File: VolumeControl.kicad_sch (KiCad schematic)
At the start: 15 parts

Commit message: some corrections
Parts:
- added C? (x2): C_Polarized 10µF 50V, symbol Device:C_Polarized
- J?: value I2C -> SPI; symbol Connector_Generic:Conn_01x02 -> Connector_Generic:Conn_01x04
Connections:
- net CLK: now also J?.1 (Pin_1), U?.5 (CLK), U?.5 (CLK)
- net GND: now also R?.1, U?.1 (B1), U?.1 (B1), U?.2 (-), U?.2 (GND), U?.2 (GND), U?.6 (-); no longer U?.3 (+)
- net SDA: now also J?.2 (Pin_2)
- net at R?.1, R?.2: now also C?.1; no longer J?.1 (Pin_1) (x2)
- net at J?.1 (Pin_1): now also C?.1; no longer U?.8 (A1)
- net at J?.3 (Pin_3): now also C?.1; no longer U?.8 (A1)
- net at C?.2: now also J?.1 (Pin_1); no longer R?.2 (x2)
- net at U?.7 (W1): now also U?.3 (+); no longer U?.2 (-)
- net SDI: now reaches U?.4 (SDI)
- net SDI: now also U?.4 (SDI)
- net at U?.7 (W1): now also U?.5 (+); no longer U?.6 (-)
- net at U?.7: now also R?.2; no longer C?.1
- new net: C?.2, U?.8 (A1) (x2)
- new net: R?.2, U?.1
- new net CS1: J?.3 (Pin_3), U?.3 (CS*)
- new net CS2: J?.4 (Pin_4), U?.3 (CS*)
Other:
- moved on the sheet: C?, R?

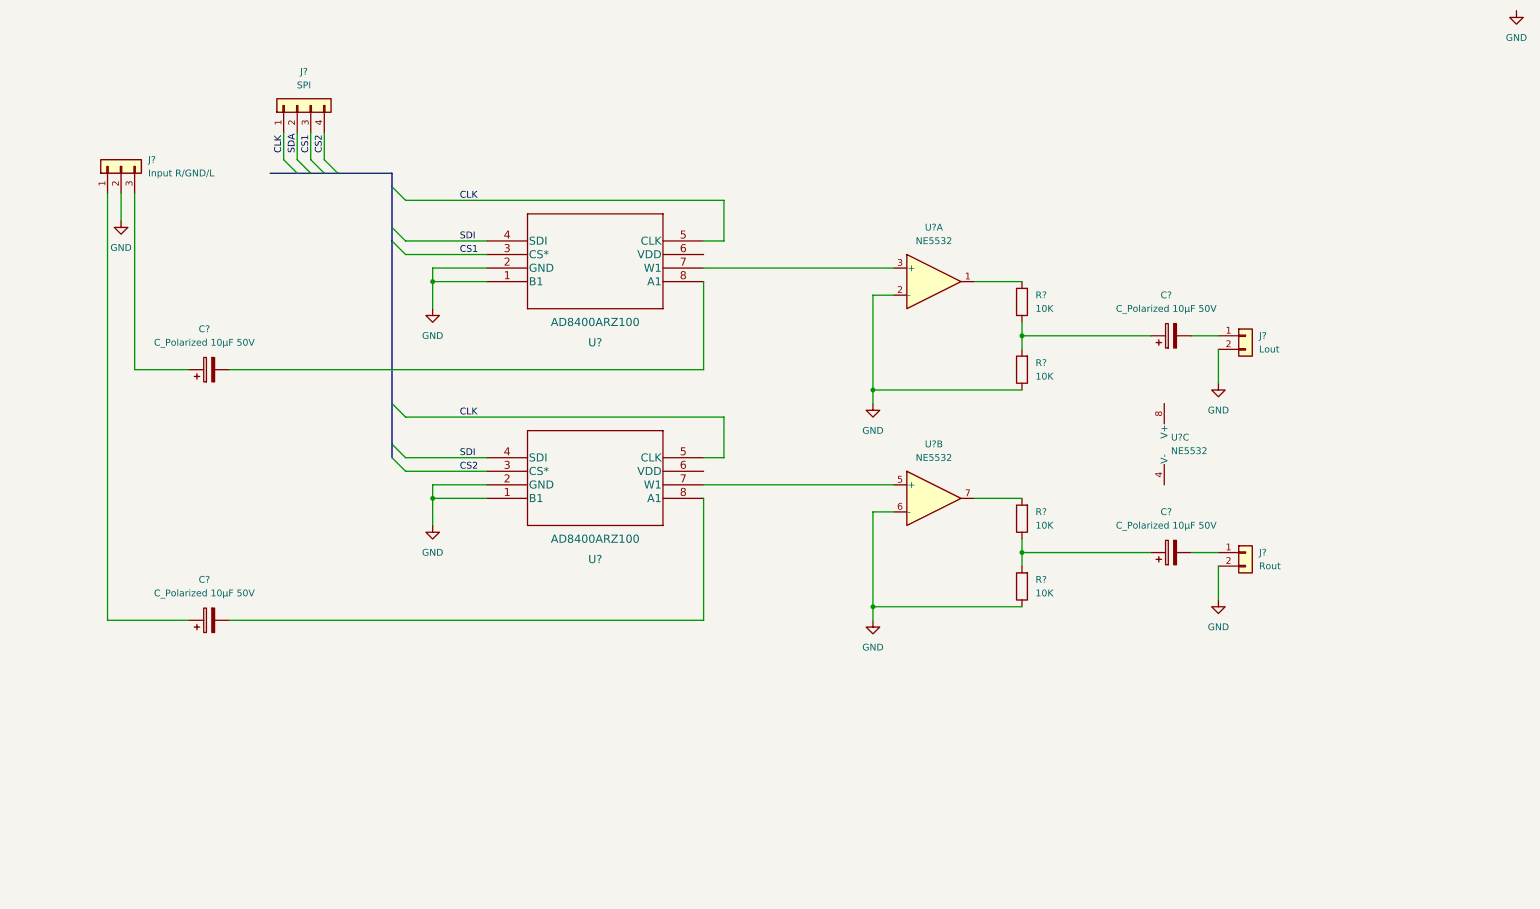
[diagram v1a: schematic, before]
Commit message: Added Sub Out
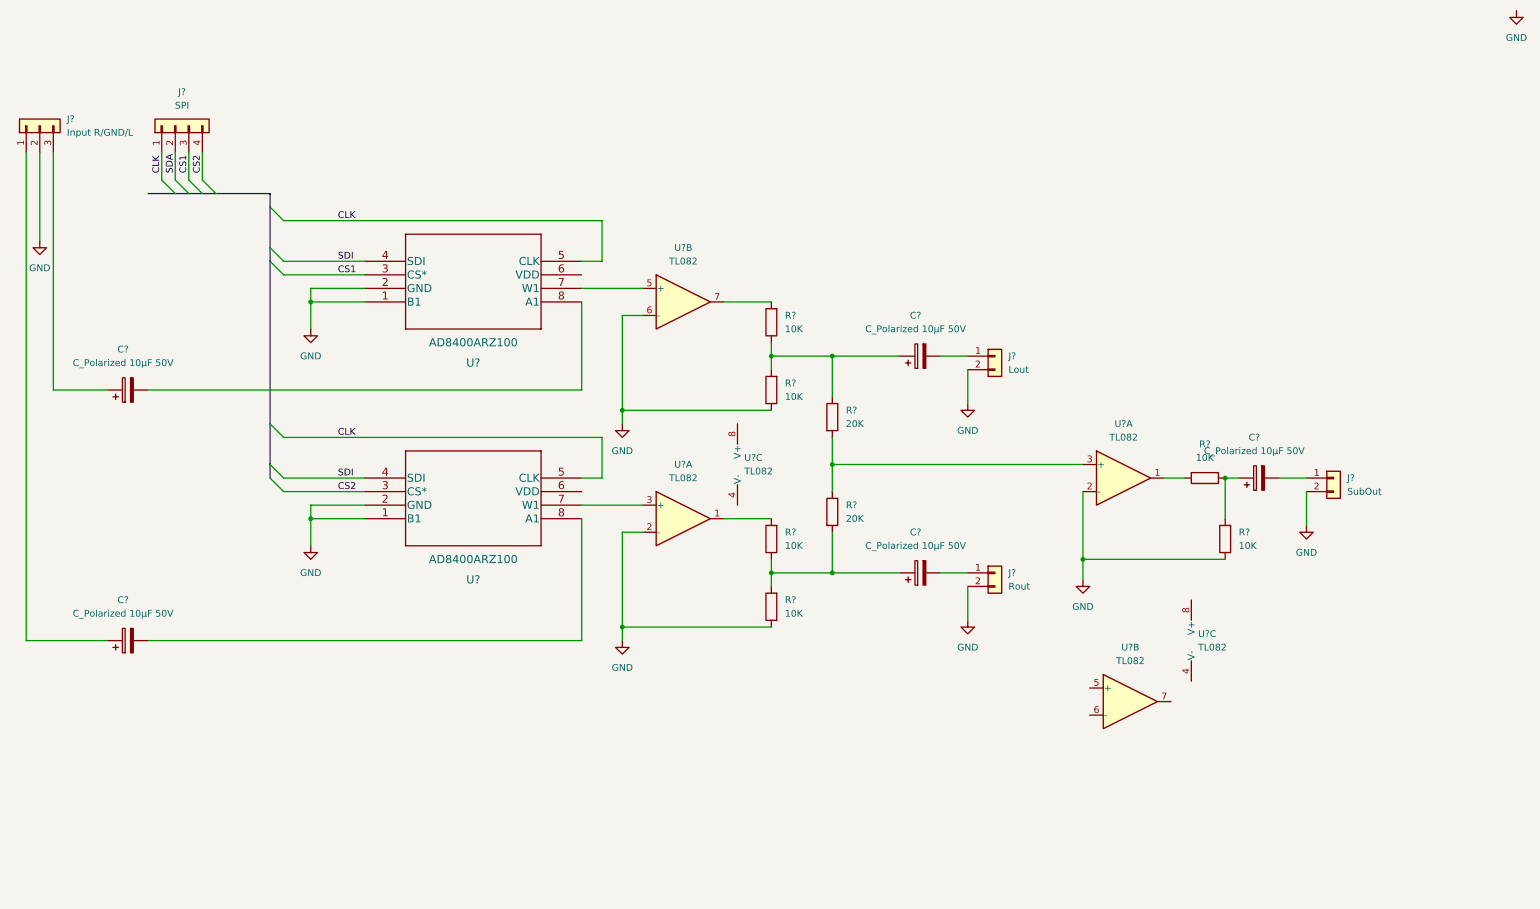
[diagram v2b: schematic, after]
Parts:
- removed U? (x3): NE5532, symbol Amplifier_Operational:NE5532
- added C?: C_Polarized 10µF 50V, symbol Device:C_Polarized
- added J?: SubOut, symbol Connector_Generic:Conn_01x02
- added R? (x2): 20K, symbol Device:R
- added R? (x2): 10K, symbol Device:R
- added U? (x6): TL082, symbol Amplifier_Operational:TL082
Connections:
- net GND: now also J?.2 (Pin_2), R?.1, U?.2 (-), U?.2 (-), U?.6 (-)
- net at C?.1, R?.1, R?.2: now also R?.1
- net at R?.2: now also U?.7
- net at U?.7 (W1): now also U?.5 (+)
- net at U?.7 (W1): now also U?.3 (+)
- net at R?.2: now also U?.1
- net at C?.1, R?.1, R?.2: now also R?.2
- new net: R?.1, R?.2, U?.3 (+)
- new net: C?.2, J?.1 (Pin_1)
- new net: C?.1, R?.1, R?.2
- new net: R?.2, U?.1
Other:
- moved on the sheet: C?, J?, R?, U?

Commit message: Added Power
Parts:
- added J?: Input R/GND/L, symbol Connector_Generic:Conn_01x03
- added J?: DP1 2.7V - 5.5V, symbol Connector_Generic:Conn_01x02
- added J?: DP2 2.7V - 5.5V, symbol Connector_Generic:Conn_01x02
- added JP?: Double or Single PSU, symbol Jumper:Jumper_3_Bridged12
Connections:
- net GND: now also J?.1 (Pin_1), J?.1 (Pin_1), J?.2 (Pin_2)
- net -2.25-40: now reaches U?.4 (V-)
- net -2.25-40: now also U?.4 (V-), J?.1 (Pin_1)
- net +2.25-40: now reaches U?.8 (V+)
- net +2.25-40: now also U?.8 (V+), J?.3 (Pin_3)
- net DP2VDD: now reaches U?.6 (VDD)
- net DP2VDD: now also JP?.2 (C)
- net DP1VDD: now reaches U?.6 (VDD)
- net DP1VDD: now also J?.2 (Pin_2), JP?.1 (A)
- new net: J?.2 (Pin_2), JP?.3 (B)

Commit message: corrected schematic, selected footprints, created pcb file
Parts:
- removed J?: Input R/GND/L, symbol Connector_Generic:Conn_01x03
- removed J?: DP2 2.7V - 5.5V, symbol Connector_Generic:Conn_01x02
- removed JP?: Double or Single PSU, symbol Jumper:Jumper_3_Bridged12
- removed R?: 10K, symbol Device:R
- added C11, C3, C9: 100n, Capacitor_THT:C_Rect_L4.6mm_W2.0mm_P2.50mm_MKS02_FKP02, symbol Device:C
- added C4, C7, C8: 1u, Capacitor_THT:C_Rect_L7.0mm_W2.5mm_P5.00mm, symbol Device:C
- added PS1: IH0512S, Converter_DCDC:Converter_DCDC_XP_POWER-IHxxxxS_THT, symbol Converter_DCDC:IH0512S
- added R1, R2, R3, R4: 100k, Resistor_THT:R_Axial_DIN0207_L6.3mm_D2.5mm_P10.16mm_Horizontal, symbol Device:R
- added R12, R13, R7: 100, Resistor_THT:R_Axial_DIN0207_L6.3mm_D2.5mm_P10.16mm_Horizontal, symbol Device:R
- C1, C10, C2, C5, C6: renamed from C?; footprint (none) -> Capacitor_THT:CP_Radial_D5.0mm_P2.00mm
- J1: renamed from J?; footprint (none) -> Connector_JST:JST_XH_B3B-XH-A_1x03_P2.50mm_Vertical
- J2: renamed from J?; footprint (none) -> Connector_PinHeader_2.54mm:PinHeader_1x04_P2.54mm_Vertical
- J4: renamed from J?; value DP1 2.7V - 5.5V -> 5V Supply; footprint (none) -> Connector_PinHeader_2.54mm:PinHeader_1x02_P2.54mm_Vertical
- J5, J6, J7: renamed from J?; footprint (none) -> Connector_Molex:Molex_KK-254_AE-6410-02A_1x02_P2.54mm_Vertical
- R10, R11, R14: renamed from R?; footprint (none) -> Resistor_THT:R_Axial_DIN0207_L6.3mm_D2.5mm_P10.16mm_Horizontal
- R5, R6: renamed from R?; value 10K -> 12k; footprint (none) -> Resistor_THT:R_Axial_DIN0207_L6.3mm_D2.5mm_P10.16mm_Horizontal
- R8, R9: renamed from R?; value 10K -> 47k; footprint (none) -> Resistor_THT:R_Axial_DIN0207_L6.3mm_D2.5mm_P10.16mm_Horizontal
- U1, U2: renamed from U?; footprint R_8_ADI -> Package_SO:SO-8_3.9x4.9mm_P1.27mm
- U3, U4: renamed from U?; footprint (none) -> Package_DIP:DIP-8_W7.62mm_Socket
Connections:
- net DP2VDD is gone; now on net +5V: U2.6 (VDD)
- net GND: now also C3.2, C4.2, C7.2, C8.1, PS1.2 (-Vin), PS1.5 (0V), R2.1; no longer U3.2 (-), U3.6 (-)
- net at C5.1, R10.1: now also R8.2, U3.7; no longer R5.2, R8.1
- net at C2.2, U2.8 (A1): now also R4.2
- net at R9.2, U3.1: now also C6.1, R11.2
- net at C10.1, R14.2: now also U4.1
- net at C1.2, U1.8 (A1): now also R3.1
- net at R6.2, R9.1: now also U3.2 (-); no longer C6.1, R11.2
- net -12VA: now reaches U4.5 (+)
- net -12VA: now also C8.2, R13.2
- net +12VA: now reaches U4.6 (-)
- net +12VA: now also C7.1, R12.1
- net +2.25-40: no longer names the net of U3.8 (V+), U4.8 (V+)
- net +2.25-40: now also C11.1, C9.1
- net -2.25-40: no longer names the net of U3.4 (V-), U4.4 (V-)
- net -2.25-40: now also C11.2, C9.2
- net DP1VDD renamed +5V
- net +5V: now also PS1.1 (+Vin), R7.2
- new net: C3.1, R1.1, R2.2, R3.2, R4.1
- new net: PS1.4 (-Vout), R13.1
- new net: PS1.6 (+Vout), R12.2
- new net: R5.2, R8.1, U3.6 (-)
- new net +5VA: C4.1, R1.2, R7.1
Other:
- note added: "Lowpass: fg~1.5KHz"
- note added: "Reichelt: RD-0512D"
- moved on the sheet: C10, C5, C6, J4, J5, J6, J7, R10, R11, R14, R5, R6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

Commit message: corrected some issues in the schematic * added jumper for phase invert of the sub out * routed layout
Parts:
- added C12, C13: 100n, Capacitor_THT:C_Rect_L4.6mm_W2.0mm_P2.50mm_MKS02_FKP02, symbol Device:C
- added C14: n.b., Capacitor_THT:C_Rect_L7.0mm_W2.5mm_P5.00mm, symbol Device:C
- added JP1: Sub out invert select, Connector_PinHeader_2.54mm:PinHeader_1x03_P2.54mm_Vertical, symbol Jumper:Jumper_3_Bridged12
- added R15, R16: 10K, Resistor_THT:R_Axial_DIN0207_L6.3mm_D2.5mm_P10.16mm_Horizontal, symbol Device:R
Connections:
- net SDA is gone; now on net SDI: J2.2 (Pin_2)
- net +12VA: now also C11.1, C9.1, U3.8 (V+), U4.8 (V+); no longer U4.6 (-)
- net +5V: now also C12.1, C13.1
- net -12VA: now also C11.2, C9.2, U3.4 (V-), U4.4 (V-); no longer U4.5 (+)
- net GND: now also U4.5 (+), C12.2, C13.2, C14.2; no longer R5.1, R6.1
- net at R10.2, R11.1, U4.3 (+): now also C14.1
- net mid: now reaches C3.1, R1.1, R2.2, R3.2, R4.1
- net mid: now also R5.1, R6.1
- net at R14.2, U4.1: now also JP1.1 (A), R15.2; no longer C10.1
- net at U4.7: now also JP1.3 (B), R16.1
- new net: C10.1, JP1.2 (C)
- new net: R15.1, R16.2, U4.6 (-)
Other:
- moved on the sheet: C10, J7, R14, U4A, U4B

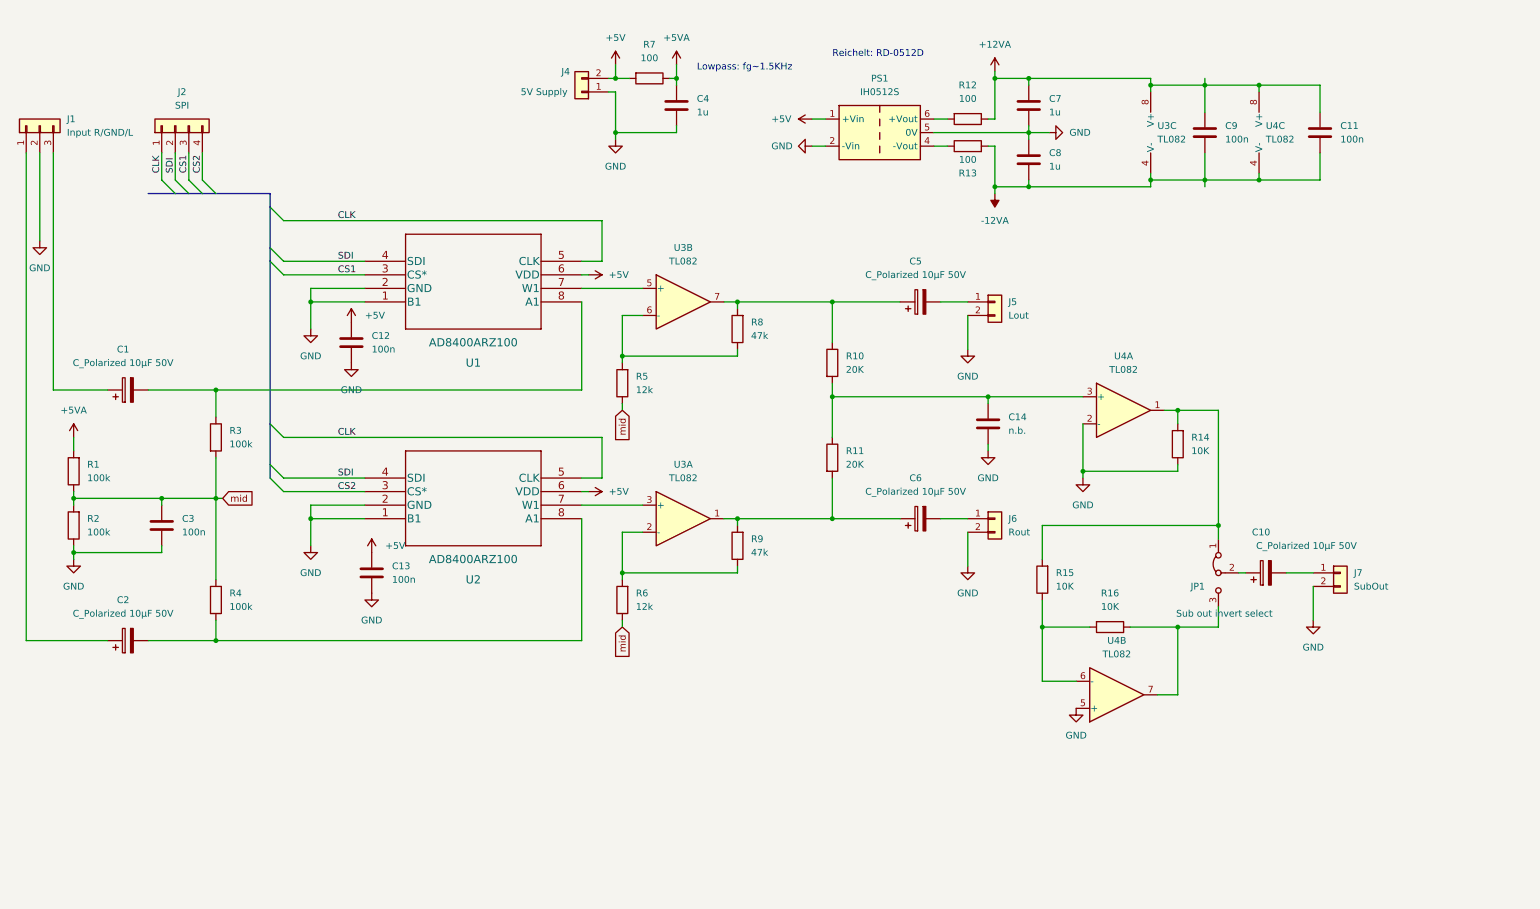
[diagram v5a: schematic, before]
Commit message: changed design to AD5290
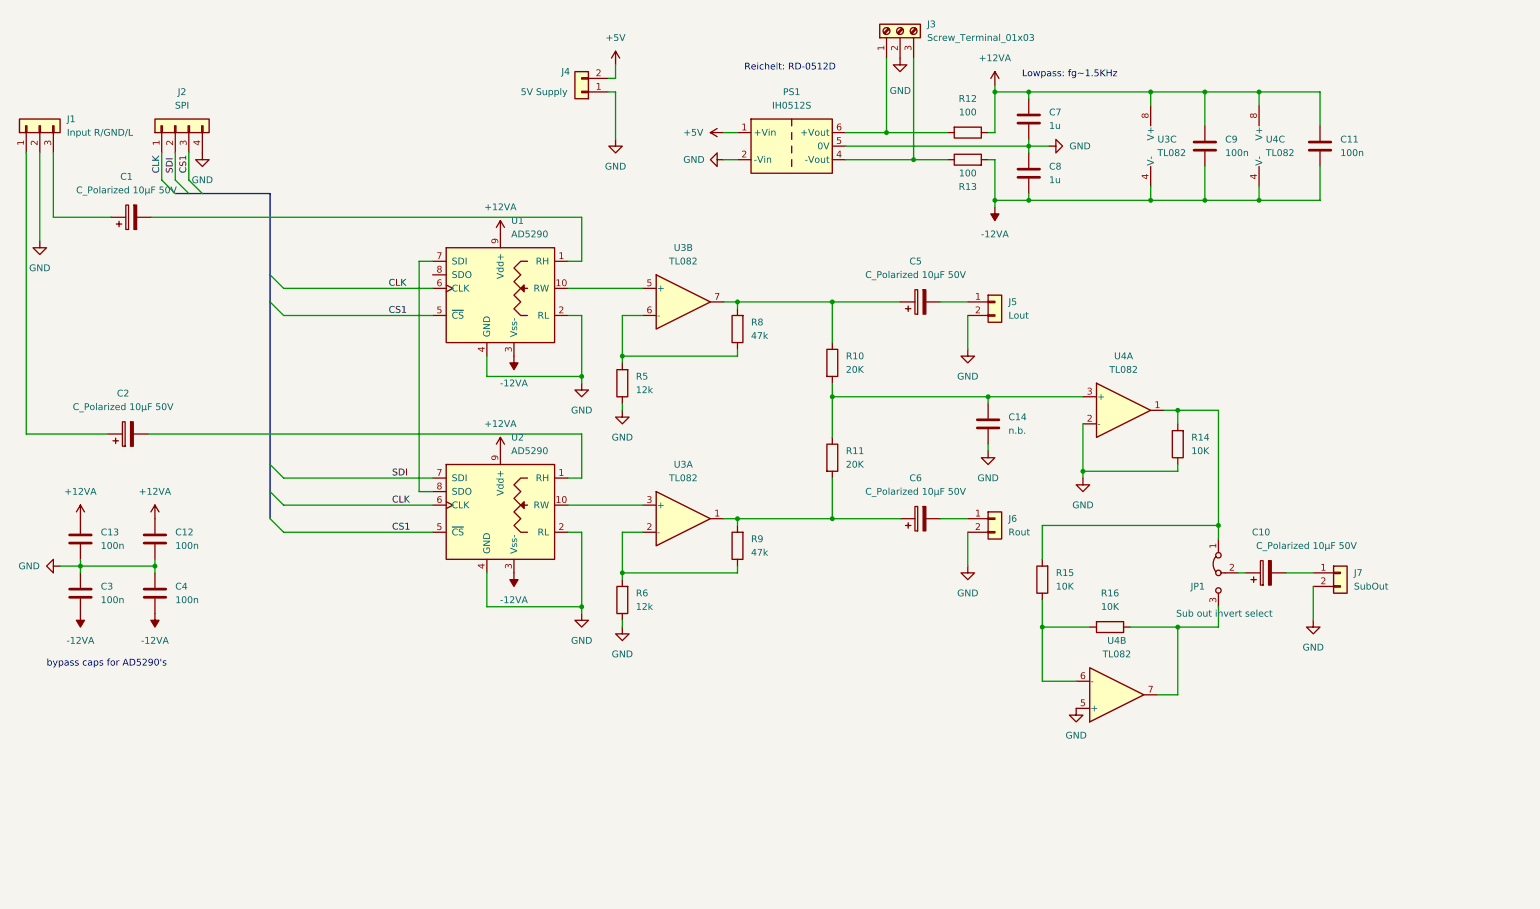
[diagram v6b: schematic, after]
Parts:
- removed R1, R2, R3, R4: 100k, Resistor_THT:R_Axial_DIN0207_L6.3mm_D2.5mm_P10.16mm_Horizontal, symbol Device:R
- removed R7: 100, Resistor_THT:R_Axial_DIN0207_L6.3mm_D2.5mm_P10.16mm_Horizontal, symbol Device:R
- removed U1, U2: AD8400ARZ100, Package_SO:SO-8_3.9x4.9mm_P1.27mm, symbol 2022-01-20_21-00-41:AD8400ARZ100
- added J3: Screw_Terminal_01x03, TerminalBlock_Phoenix:TerminalBlock_Phoenix_PT-1,5-3-5.0-H_1x03_P5.00mm_Horizontal, symbol Connector:Screw_Terminal_01x03
- added U1, U2: AD5290, Package_SO:MSOP-10_3x3mm_P0.5mm, symbol Potentiometer_Digital:AD5290
- C4: value 1u -> 100n; footprint Capacitor_THT:C_Rect_L7.0mm_W2.5mm_P5.00mm -> Capacitor_THT:C_Rect_L4.6mm_W2.0mm_P2.50mm_MKS02_FKP02
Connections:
- net +5VA is gone; now on net GND: C4.1
- net CS2 is gone; now on net GND: J2.4 (Pin_4)
- net mid is gone; now on net GND: C3.1, R5.1, R6.1
- net +12VA: now also C12.1, C13.1, U1.9 (Vdd+), U2.9 (Vdd+)
- net +5V: no longer C12.1, C13.1
- net -12VA: now also C3.2, C4.2, U1.3 (Vss-), U2.3 (Vss-)
- net CLK: now also U1.6 (CLK), U2.6 (CLK)
- net CS1: now also U1.5 (~{CS}), U2.5 (~{CS})
- net GND: now also J3.2 (Pin_2), U1.2 (RL), U1.4 (GND), U2.2 (RL), U2.4 (GND); no longer C3.2, C4.2
- net SDI: now also U2.7 (SDI)
- net at C2.2: now also U2.1 (RH)
- net at PS1.4 (-Vout), R13.1: now also J3.3 (Pin_3)
- net at PS1.6 (+Vout), R12.2: now also J3.1 (Pin_1)
- net at U3.3 (+): now also U2.10 (RW)
- net at U3.5 (+): now also U1.10 (RW)
- net at C1.2: now also U1.1 (RH)
- new net: U1.7 (SDI), U2.8 (SDO)
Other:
- note added: "bypass caps for AD5290's"
- moved on the sheet: C1, C11, C12, C13, C2, C7, C8, C9, PS1, R12, R13, U3C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
